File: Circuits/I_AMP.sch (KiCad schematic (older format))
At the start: 43 parts, among them P1 INPUT, P2 OUTPUT (0-5V), P3 +8, P4 -8, P5 GND, P6 GAIN_ADJ., U1 TL062, U2 OPA177, U3 LM393

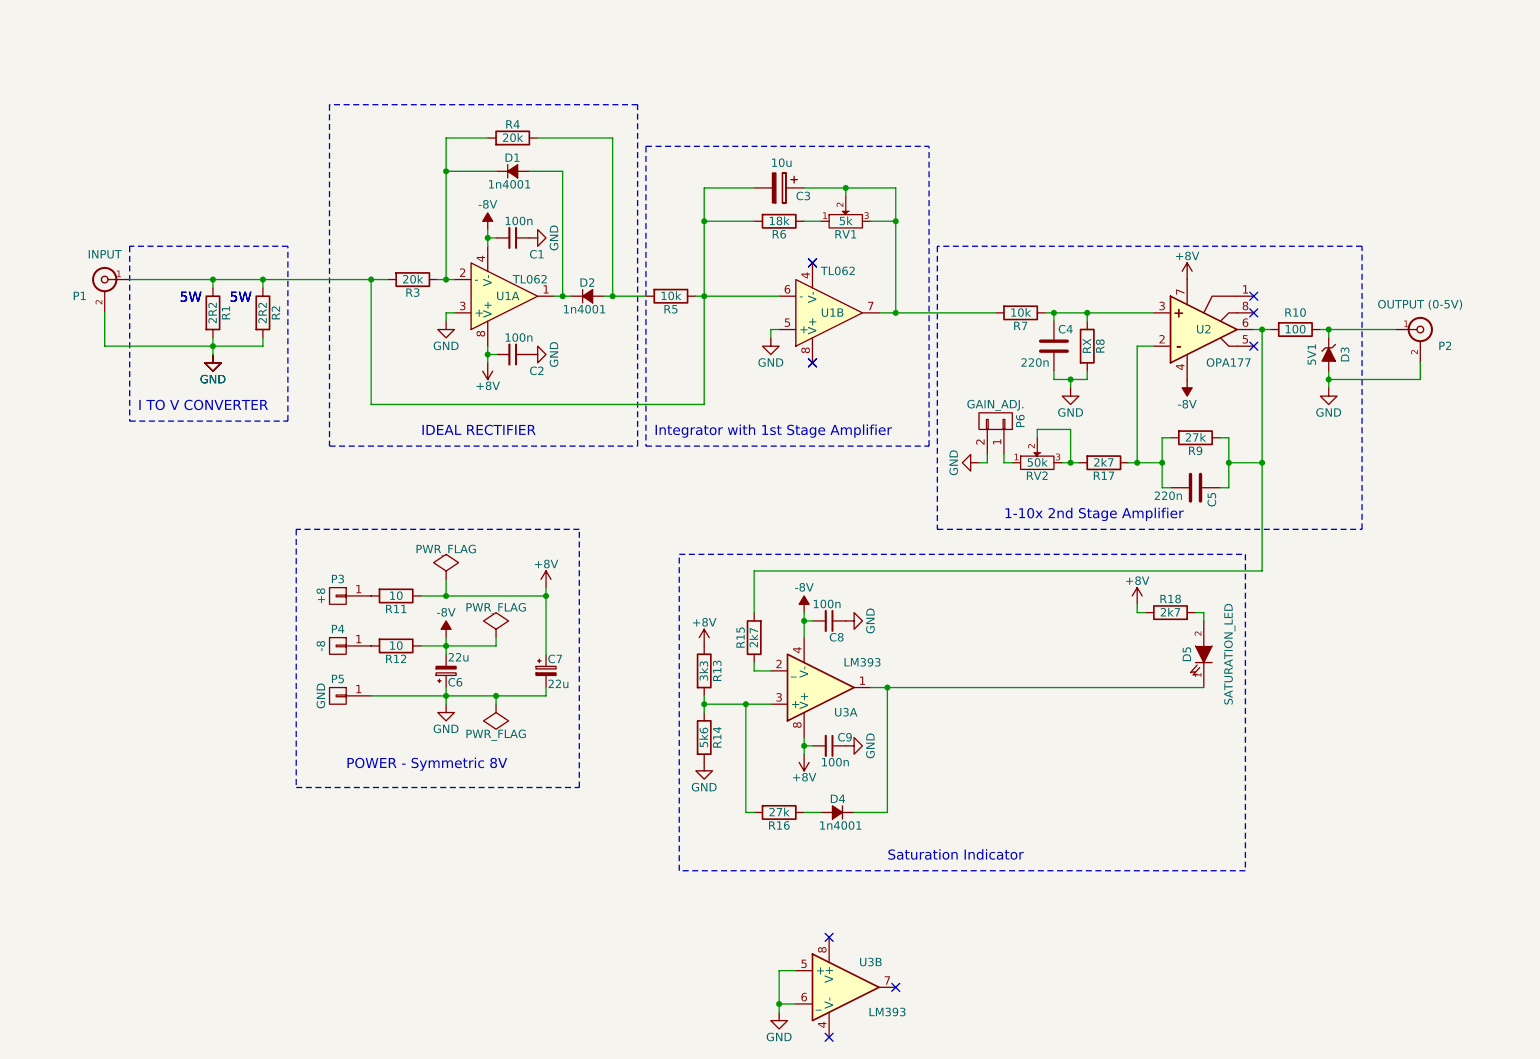
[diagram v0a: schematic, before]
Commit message: Adicionada fonte de corrente e corrigido sensor de corrente
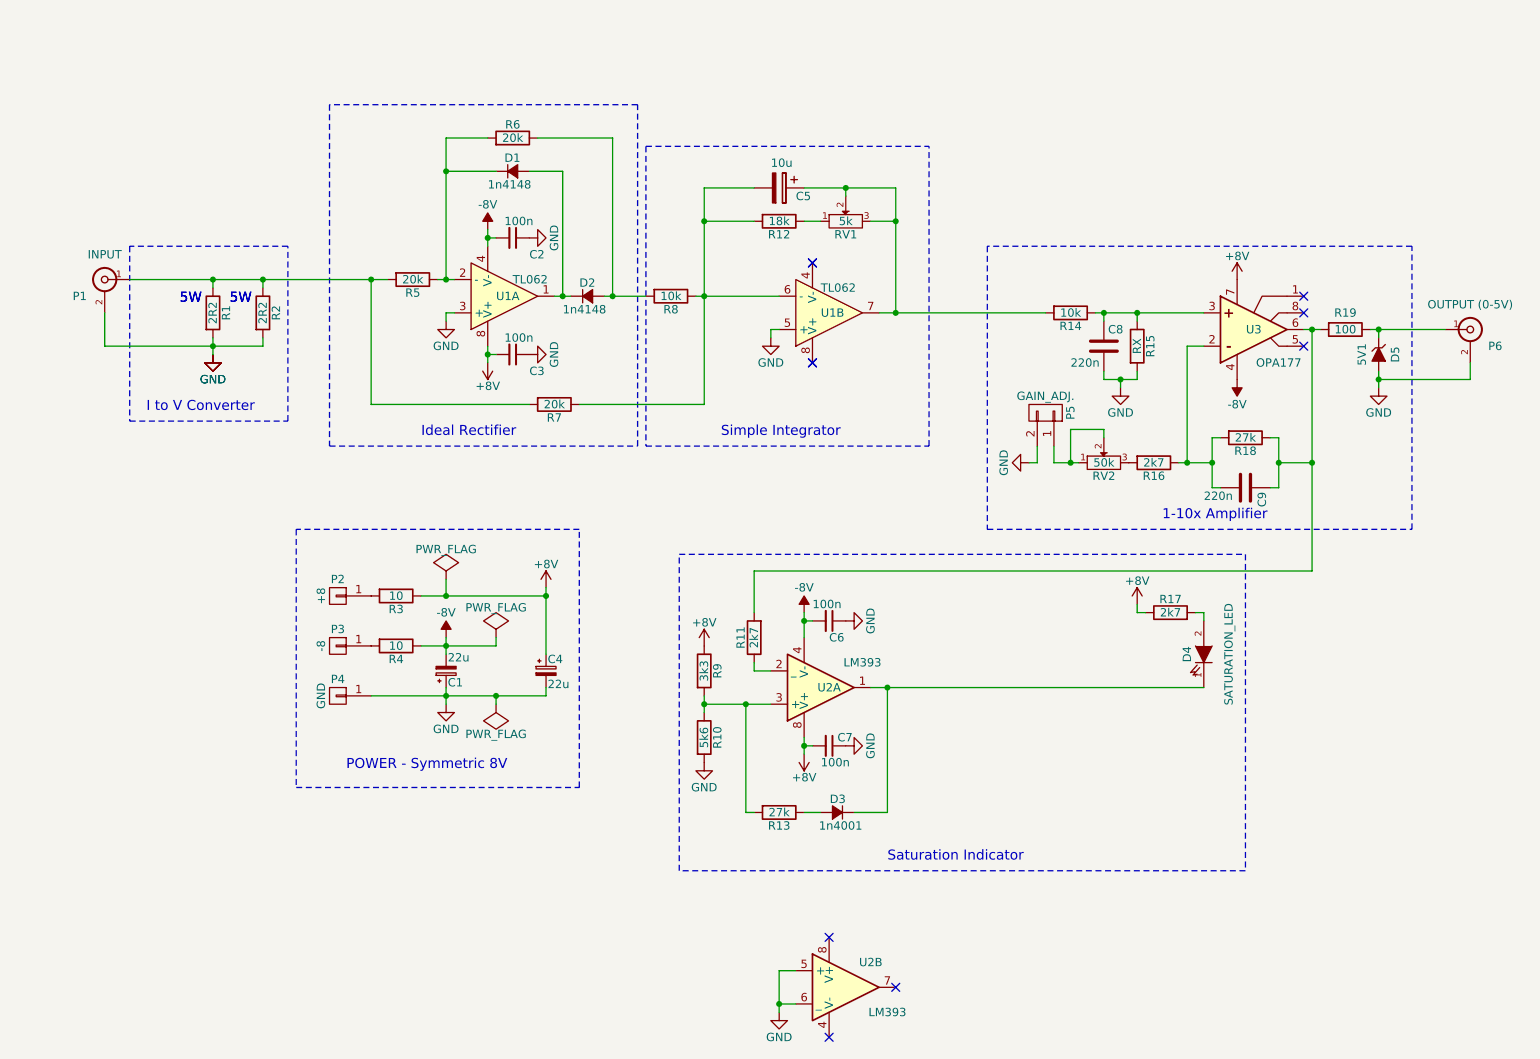
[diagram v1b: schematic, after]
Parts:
- added R7: 20k, symbol R
- D1, D2: value 1n4001 -> 1n4148
- renumbered C6 to C1, C1 to C2, C2 to C3, C7 to C4, C3 to C5, C8 to C6, C9 to C7, C4 to C8, C5 to C9, D4 to D3, D5 to D4, D3 to D5, P3 to P2, P4 to P3, P5 to P4, P6 to P5, P2 to P6, R14 to R10, R15 to R11, R6 to R12, R16 to R13, R7 to R14, R8 to R15, R17 to R16, R18 to R17, R9 to R18, R10 to R19, R11 to R3, R12 to R4, R3 to R5, R4 to R6, R5 to R8, R13 to R9, U3 to U2, U2 to U3
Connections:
- net at P1.1 (In), R1.1, R2.1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: now also R7.2; no longer C5.2, R12.2, R8.1, U1.6 (-)
- net at R16.2, RV2.3: no longer RV2.2
- net at P5.1 (P1), RV2.1: now also RV2.2
- new net: C5.2, R12.2, R7.1, R8.1, U1.6 (-)
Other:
- note added: "1-10x Amplifier\n"
- note added: "I to V Converter\n"
- note added: "Ideal Rectifier"
- note added: "Simple Integrator\n"
- note removed: "1-10x 2nd Stage Amplifier\n"
- note removed: "I TO V CONVERTER\n"
- note removed: "IDEAL RECTIFIER"
- note removed: "Integrator with 1st Stage Amplifier"
- moved on the sheet: C8, C9, D5, P5, P6, R14, R15, R16, R18, R19, RV2, U3

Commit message: ADD: Schematic Documentation
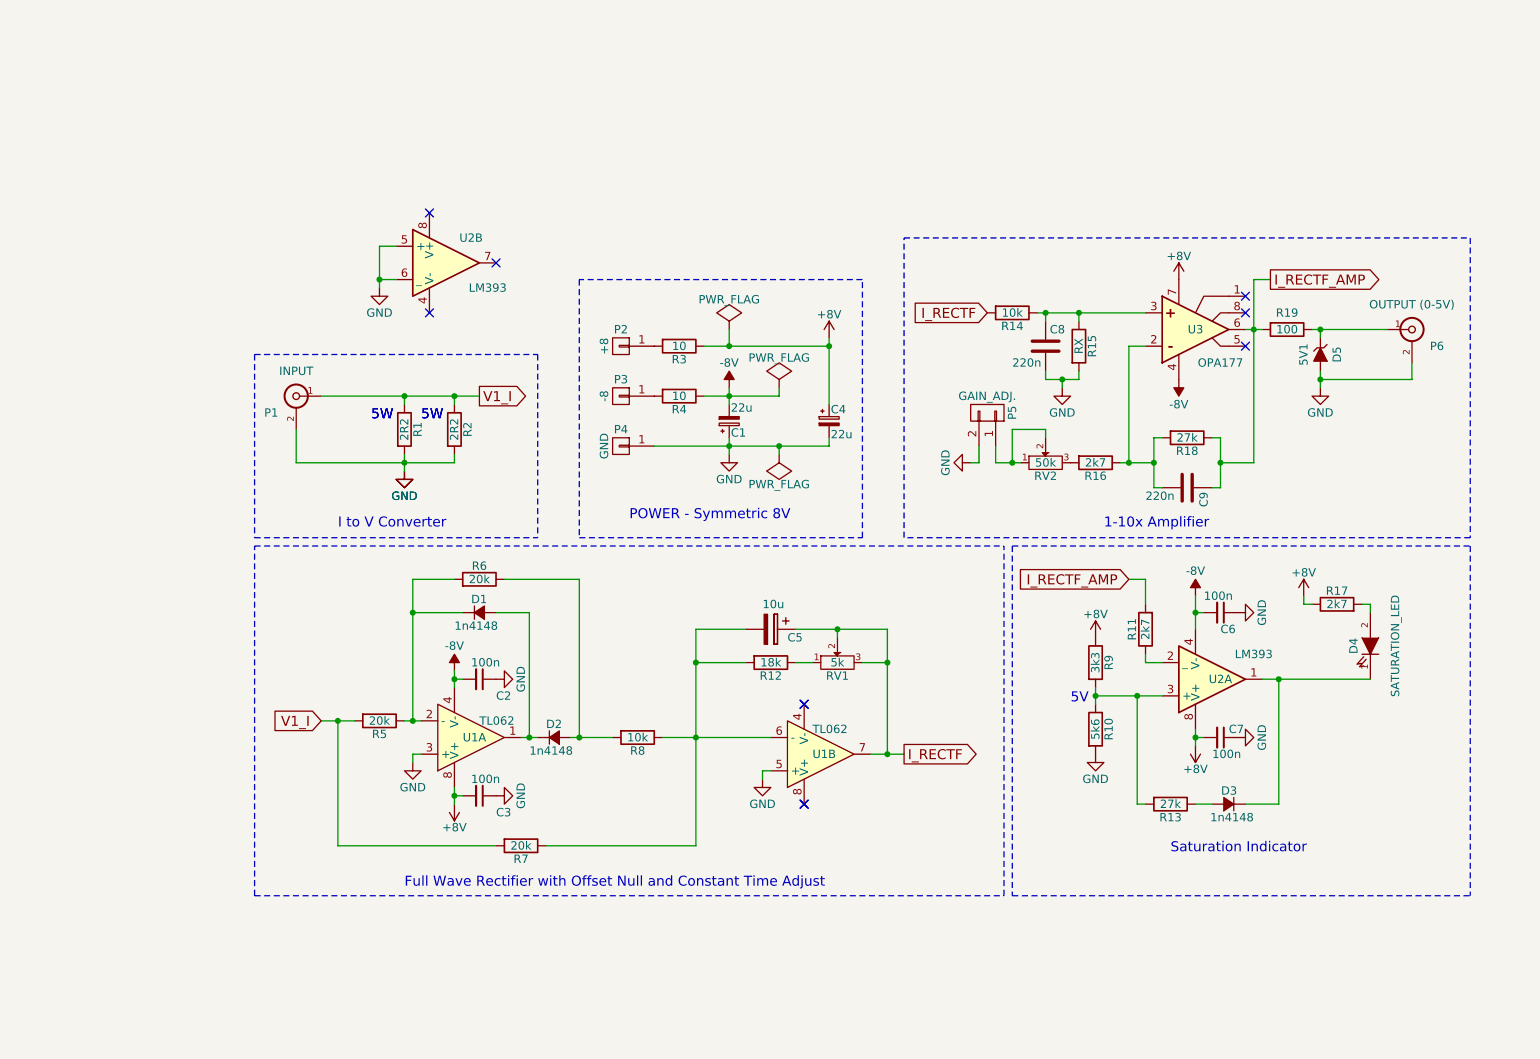
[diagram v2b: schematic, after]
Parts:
- D3: value 1n4001 -> 1n4148
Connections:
- net V1_I: now reaches P1.1 (In), R1.1, R2.1, R5.2, R7.2
- net I_RECTF: now reaches C5.1, R14.2, RV1.2, RV1.3, U1.7
- net I_RECTF_AMP: now reaches C9.1, R11.2, R18.1, R19.2, U3.6 (OUTPUT)
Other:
- note added: "5V"
- note added: "Full Wave Rectifier with Offset Null and Constant Time Adjust\n\n\n"
- note removed: "Ideal Rectifier"
- note removed: "Simple Integrator\n"
- moved on the sheet: C1, C2, C3, C4, C5, C6, C7, C8, C9, D1, D2, D3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

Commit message: Added full schematics and power supply
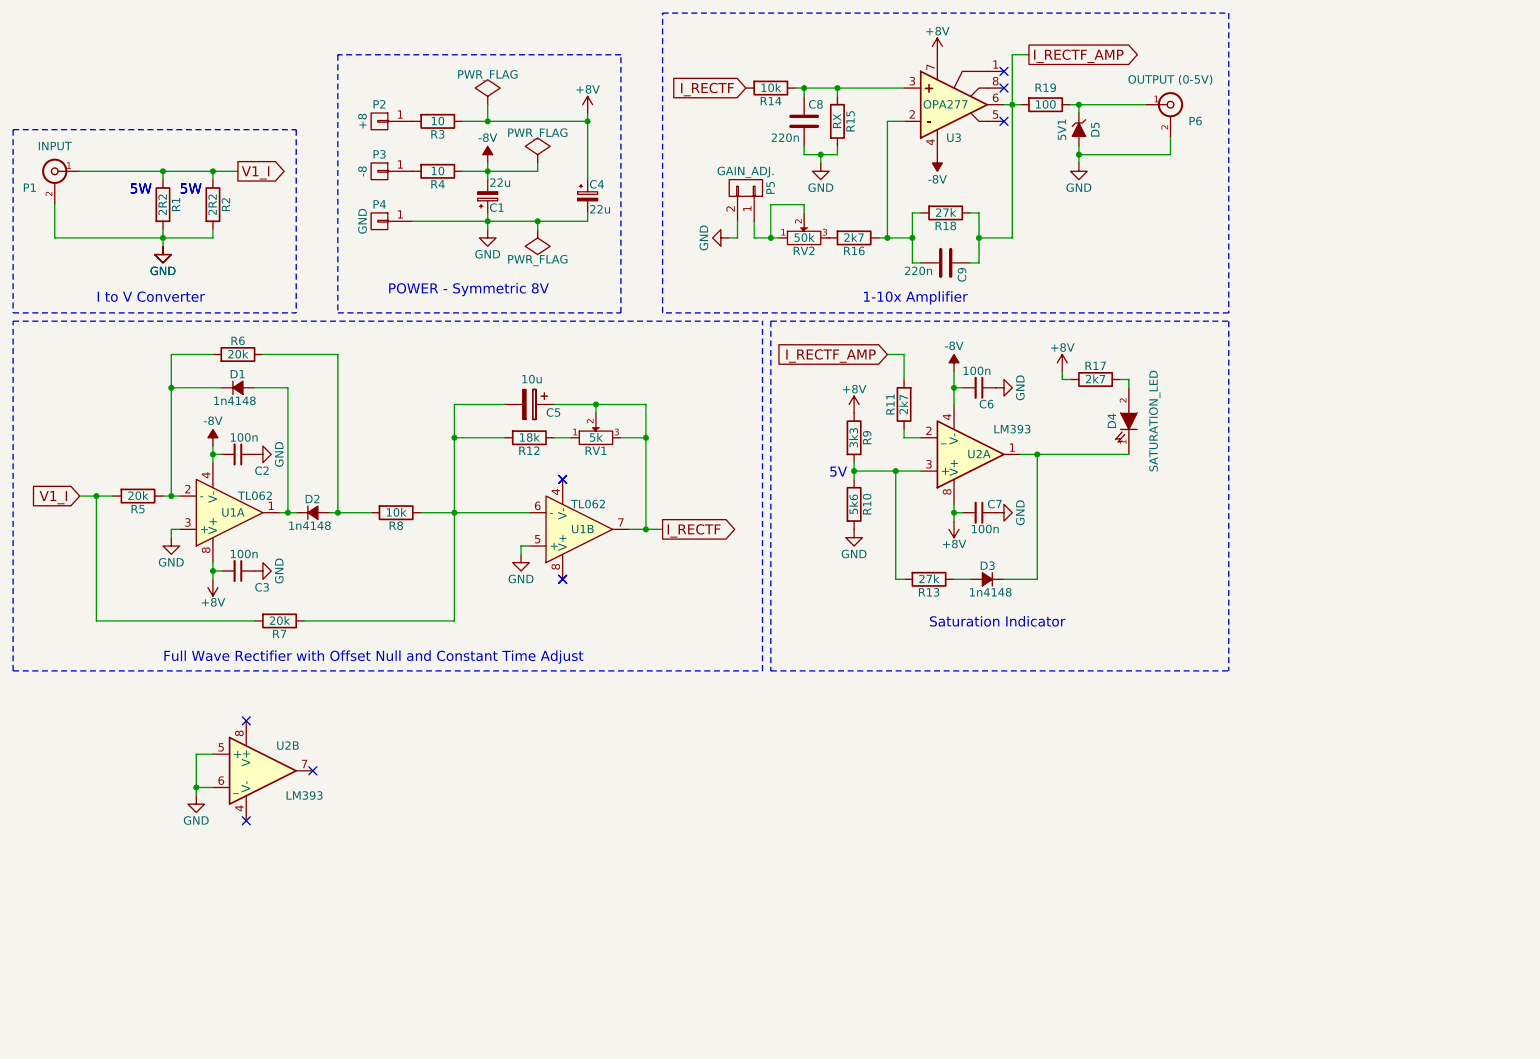
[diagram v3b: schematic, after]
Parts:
- U3: value OPA177 -> OPA277
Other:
- moved on the sheet: C1, C2, C3, C4, C5, C6, C7, C8, C9, D1, D2, D3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
